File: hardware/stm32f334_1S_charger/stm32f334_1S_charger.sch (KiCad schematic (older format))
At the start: 22 parts

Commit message: schematic revision 1 - all parts and footprint + software frame-work
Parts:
- removed D?: D_Schottky, symbol Device:D_Schottky
- removed Q?: Q_NMOS_DGS, symbol Device:Q_NMOS_DGS
- added C1, C10, C11, C9: 100n, Capacitor_SMD:C_1206_3216Metric_Pad1.42x1.75mm_HandSolder, symbol Device:C_Small
- added C15, C18, C19, C2, C20, C21, C8: 1n, Capacitor_SMD:C_1206_3216Metric_Pad1.42x1.75mm_HandSolder, symbol Device:C_Small
- added C3: 100u/16V, Capacitor_THT:CP_Radial_D6.3mm_P2.50mm, symbol Device:C_Small
- added C6: C1206C475K5RACTU, Capacitor_SMD:C_1206_3216Metric_Pad1.42x1.75mm_HandSolder, symbol Device:C_Small
- added D1, D4: B540C-13-F, Diode_SMD:D_SMC_Handsoldering, symbol Device:D_Schottky
- added D2, D3, D5, D6: APTD3216SURCK, LED_SMD:LED_1206_3216Metric, symbol Device:LED_Small
- added J2: Conn_01x05, Connector_PinHeader_2.54mm:PinHeader_1x05_P2.54mm_Vertical, symbol Connector_Generic:Conn_01x05
- added J3: Conn_01x10, Connector_PinHeader_2.54mm:PinHeader_1x10_P2.54mm_Vertical, symbol Connector_Generic:Conn_01x10
- added Q1: BUK9M52-40E, Package_TO_SOT_SMD:LFPAK33, symbol stm32f334_1S_charger:BUK9M52-40E
- added R1, R11, R17, R18, R2, R3: 10k, Resistor_SMD:R_1206_3216Metric_Pad1.42x1.75mm_HandSolder, symbol Device:R_Small
- added R13, R14, R15, R16, R4, R5: 1k, Resistor_SMD:R_1206_3216Metric_Pad1.42x1.75mm_HandSolder, symbol Device:R_Small
- added R6, R7: DNP, Resistor_SMD:R_1206_3216Metric_Pad1.42x1.75mm_HandSolder, symbol Device:R_Small
- added TH1: NCP21XV103J03RA, Resistor_SMD:R_0805_2012Metric_Pad1.15x1.40mm_HandSolder, symbol Device:Thermistor_NTC
- added U1: VXO7805-1000, stm32f334_1S_charger:VXO7805-1000, symbol stm32f334_1S_charger:VXO7805-1000
- added U2: MIC5504-3.3YM5, Package_TO_SOT_SMD:SOT-23-5, symbol Regulator_Linear:MIC5504-3.3YM5
- C12, C13, C14: renamed from C?; value C_Small -> C1206C475K5RACTU; footprint (none) -> Capacitor_SMD:C_1206_3216Metric_Pad1.42x1.75mm_HandSolder
- C16: renamed from C?; value C_Small -> 1000u/16V; footprint (none) -> Capacitor_THT:CP_Radial_D10.0mm_P5.00mm
- C17, C5: renamed from C?; value C_Small -> 100n; footprint (none) -> Capacitor_SMD:C_1206_3216Metric_Pad1.42x1.75mm_HandSolder
- C4: renamed from C?; value C_Small -> 1000u/25V; footprint (none) -> Capacitor_THT:CP_Radial_D13.0mm_P5.00mm
- C7: renamed from C?; value C_Small -> 1n; footprint (none) -> Capacitor_SMD:C_1206_3216Metric_Pad1.42x1.75mm_HandSolder
- F1: renamed from F?; value Fuse_Small -> 0697H6300-01; footprint (none) -> stm32f334_1S_charger:0697H6300-01
- J1: renamed from J?; footprint (none) -> Connector_PinHeader_2.54mm:PinHeader_1x02_P2.54mm_Vertical
- J4: renamed from J?; value BATTERYU -> BATTERY; footprint (none) -> stm32f334_1S_charger:18650_holder
- L1: renamed from L?; value L_Small -> SRR1210-121M; footprint (none) -> Inductor_SMD:L_Bourns_SRR1210A
- L2: renamed from L?; value L_Small -> SRR1210-560M; footprint (none) -> Inductor_SMD:L_Bourns_SRR1210A
- R10, R12: renamed from R?; footprint (none) -> Resistor_SMD:R_1206_3216Metric_Pad1.42x1.75mm_HandSolder
- R8: renamed from R?; value R_Small -> 4.7; footprint (none) -> Resistor_SMD:R_1206_3216Metric_Pad1.42x1.75mm_HandSolder
- R9: renamed from R?; value R_Small -> 47; footprint (none) -> Resistor_SMD:R_1206_3216Metric_Pad1.42x1.75mm_HandSolder
- U4: renamed from U?; footprint (none) -> stm32f334_1S_charger:SC70-6
- U5: renamed from U?; footprint (none) -> Package_TO_SOT_SMD:SOT-23-5_HandSoldering
- gave numbers to parts that had none: 1
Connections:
- net HTRIM_OUT is gone; now on net HTRIM_CHA1: U5.3 (IN+)
- net I_PK_SENSE is gone; now on net COMP2_INP: C7.2, R9.2
- net I_SENSE is gone; now on net ADC1_IN2: U4.6 (OUT)
- net +3V3: now also U3.1 (VDD), U3.17 (VDD), U3.5 (VDDA), C10.2, C11.2, C6.2, C9.2, R1.1, R11.1, R7.2, U2.5 (VOUT)
- net +5V: now also C1.2, C3.2, R6.2, U1.3 (VOUT), U2.1 (VIN), U2.3 (EN)
- net GND: now also C1.1, C10.1, C11.1, C15.1, C19.1, C2.1, C20.1, C21.1, C3.1, C6.1, C8.1, C9.1, D2.1 (K), D3.1 (K), D5.1 (K), D6.1 (K), J2.5 (Pin_5), J3.10 (Pin_10), R18.2, R2.2, R5.2, TH1.2, U1.2 (GND), U2.2 (GND); no longer C7.1
- net DAC1_OUT: now reaches U3.10 (PA4)
- net DAC1_OUT: now also C21.2
- net COMP2_INP: now reaches U3.13 (PA7)
- net PB0: now reaches U3.14 (PB0)
- net PB0: now also J3.3 (Pin_3)
- net PB1: now reaches U3.15 (PB1)
- net PB1: now also J3.4 (Pin_4)
- net HTRIM_CHA1: now reaches U3.18 (PA8)
- net LED1: now reaches U3.19 (PA9)
- net LED1: now also R16.1
- net LED2: now reaches U3.20 (PA10)
- net LED2: now also R15.1
- net LED3: now reaches U3.21 (PA11)
- net LED3: now also R14.1
- net LED4: now reaches U3.22 (PA12)
- net LED4: now also R13.1
- net JTAG_SWDIO: now reaches U3.23 (PA13)
- net JTAG_SWDIO: now also J2.2 (Pin_2)
- net JTAG_SWCLK: now reaches U3.24 (PA14)
- net JTAG_SWCLK: now also J2.3 (Pin_3)
- net PB3: now reaches U3.26 (PB3)
- net PB3: now also J3.5 (Pin_5)
- net PB4: now reaches U3.27 (PB4)
- net PB4: now also J3.6 (Pin_6)
- net PB5: now reaches U3.28 (PB5)
- net PB5: now also J3.7 (Pin_7)
- net PB6: now reaches U3.29 (PB6)
- net PB6: now also J3.8 (Pin_8)
- net PB7: now reaches U3.30 (PB7)
- net PB7: now also J3.9 (Pin_9)
- net at U3.31 (BOOT0): now also J2.4 (Pin_4), R2.1
- net NRST: now reaches U3.4 (NRST)
- net NRST: now also J2.1 (Pin_1), R1.2
- net ADC1_IN1: now reaches U3.6 (PA0)
- net ADC1_IN1: now also C20.2, R17.2, R18.1
- net ADC1_IN2: now reaches U3.7 (PA1)
- net ADC1_IN2: now also C18.2
- net ADC1_IN3: now reaches U3.8 (PA2)
- net ADC1_IN3: now also C2.2, R3.2, R4.1
- net ADC1_IN4: now reaches U3.9 (PA3)
- net ADC1_IN4: now also C15.2, R11.2, TH1.1
- net at C16.1, C17.1, R12.2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: now also D1.1 (K)
- net at R12.1, U4.5 (IN-): now also D4.2 (A); no longer J4.1 (Pin_1)
- net at C12.1, C13.1, C14.1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: now also D1.2 (A)
- net at C12.2, C13.2, C14.2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: now also Q1.5 (D)
- net at R8.1: now also Q1.4 (G)
- net at R10.2, R9.1: now also Q1.1 (S), Q1.2 (S), Q1.3 (S)
- net POWER_MAIN renamed +12V
- net +12V: now also R3.1, U1.1 (VCC)
- new net: D4.1 (K), J4.1 (Pin_1), R17.1
- new net: C7.1, C8.2
- new net: R4.2, R5.1
- new net: C18.1, C19.2
- new net: J3.1 (Pin_1), R6.1
- new net: J3.2 (Pin_2), R7.1
- new net: D2.2 (A), R13.2
- new net: D3.2 (A), R14.2
- new net: D5.2 (A), R15.2
- new net: D6.2 (A), R16.2
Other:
- note added: "2.1V @ 4.2V"
- note added: "2V@12V"
- note added: "3V@3A"
- note added: "BAT TSENSE"
- note added: "CONTROL SECTION"
- note added: "EXTERNAL COMMUNICATION"
- note added: "LOW VOLTAGE POWER SUPPLY"
- note added: "POWER CONVERSION SECTION"
- note added: "STATUS INDICATOR LEDS"
- moved on the sheet: C12, C13, C14, C16, C17, C4, C5, C7, F1, J1, J4, L1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

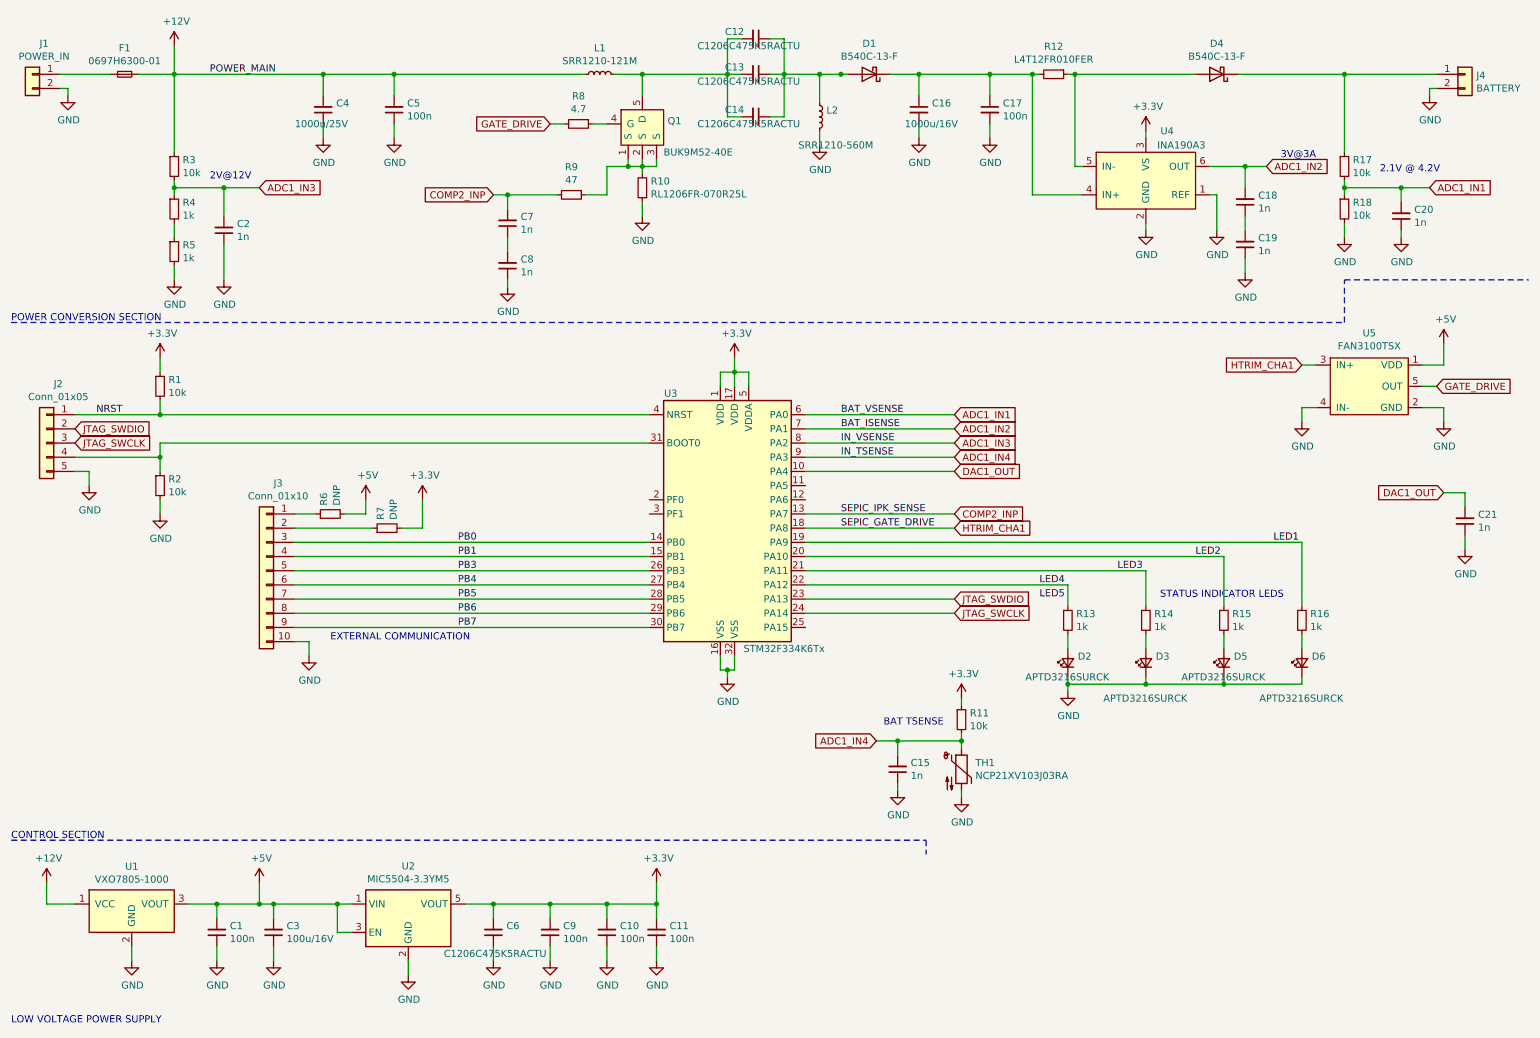
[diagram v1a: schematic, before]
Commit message: v1.0 board, pre-production
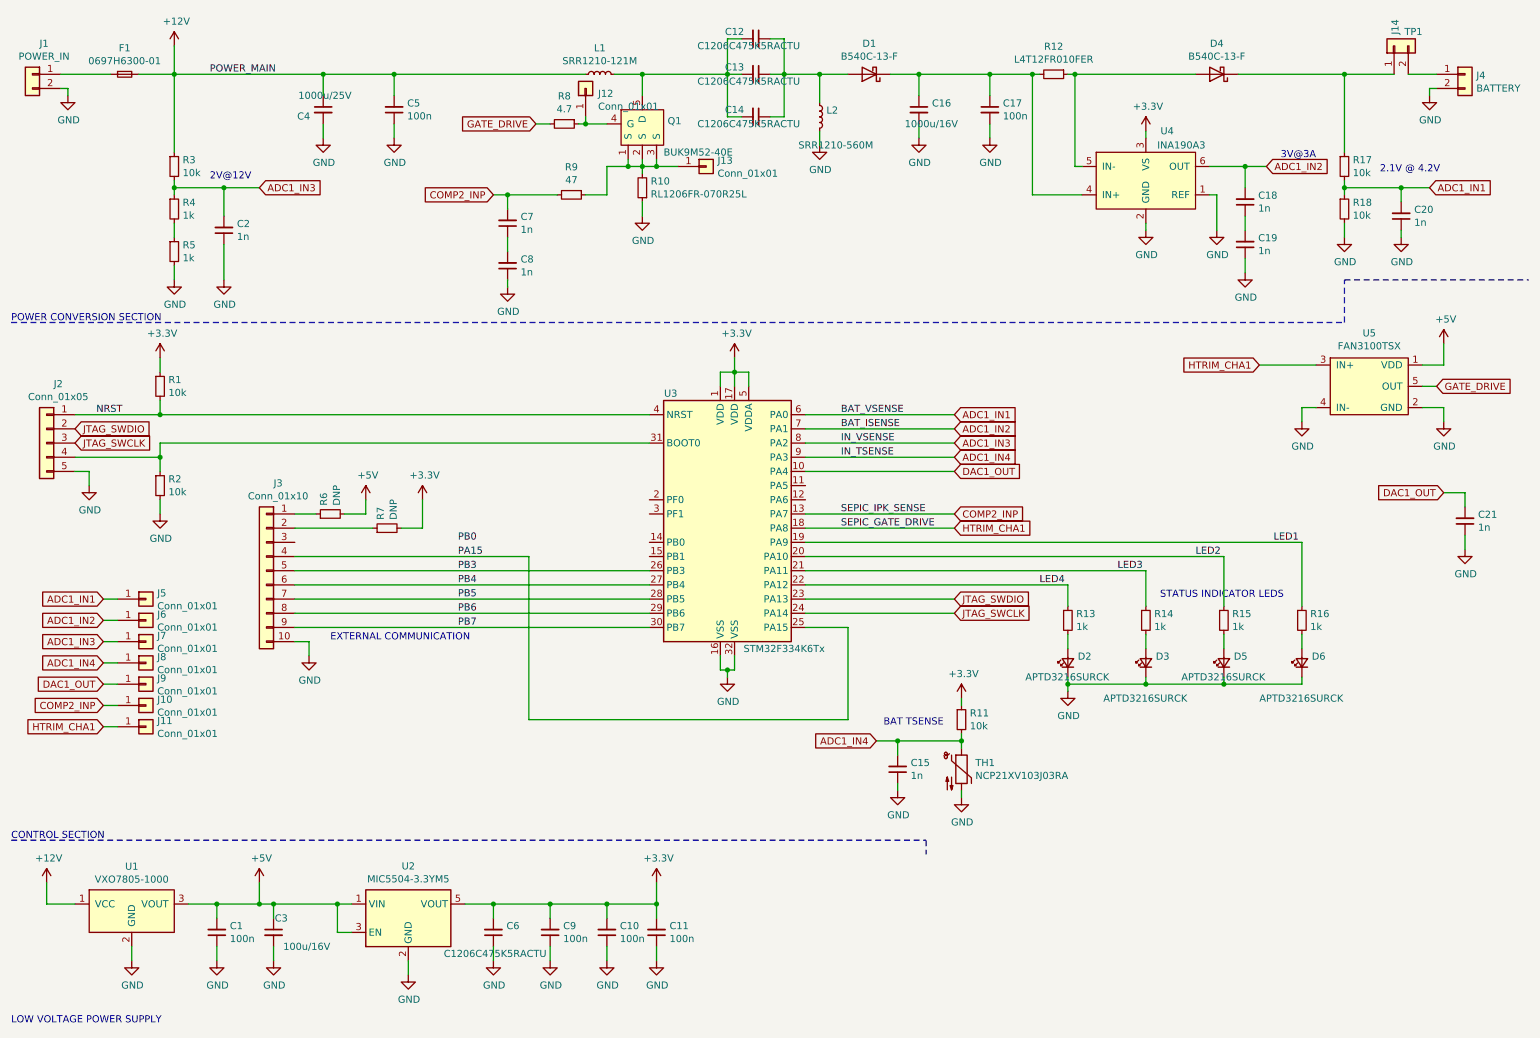
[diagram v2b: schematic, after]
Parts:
- added J10, J11, J12, J13, J5, J6, J7, J8, J9: Conn_01x01, Connector_PinHeader_2.54mm:PinHeader_1x01_P2.54mm_Vertical, symbol Connector_Generic:Conn_01x01
- added J14: TP1, Connector_PinHeader_2.54mm:PinHeader_1x02_P2.54mm_Vertical, symbol Connector_Generic:Conn_01x02
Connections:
- net +12V: now also C4.1; no longer C4.2
- net +5V: now also C3.1; no longer C3.2
- net ADC1_IN1: now also J5.1 (Pin_1)
- net ADC1_IN2: now also J6.1 (Pin_1)
- net ADC1_IN3: now also J7.1 (Pin_1)
- net ADC1_IN4: now also J8.1 (Pin_1)
- net COMP2_INP: now also J10.1 (Pin_1)
- net DAC1_OUT: now also J9.1 (Pin_1)
- net GND: now also C3.2, C4.2; no longer C3.1, C4.1
- net HTRIM_CHA1: now also J11.1 (Pin_1)
- net PB0: no longer J3.3 (Pin_3), U3.14 (PB0)
- net PA15: now reaches U3.25 (PA15)
- net PA15: now also J3.4 (Pin_4)
- net at D4.1 (K), R17.1: now also J14.1 (Pin_1); no longer J4.1 (Pin_1)
- net at Q1.1 (S), Q1.2 (S), Q1.3 (S)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: now also J13.1 (Pin_1)
- net at Q1.4 (G), R8.1: now also J12.1 (Pin_1)
- net PB1: no longer names the net of U3.15 (PB1)
- net PB1: no longer J3.4 (Pin_4)
- new net: J14.2 (Pin_2), J4.1 (Pin_1)
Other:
- moved on the sheet: R8
